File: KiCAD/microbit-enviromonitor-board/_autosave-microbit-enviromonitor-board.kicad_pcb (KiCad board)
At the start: 2 copper layers, 45.7 x 62.2 mm, 12 parts, among them J1 12V, J2 SERIAL, J3 3V3, J4 PUMP, Q1 TIP41C, U1 REGULATOR

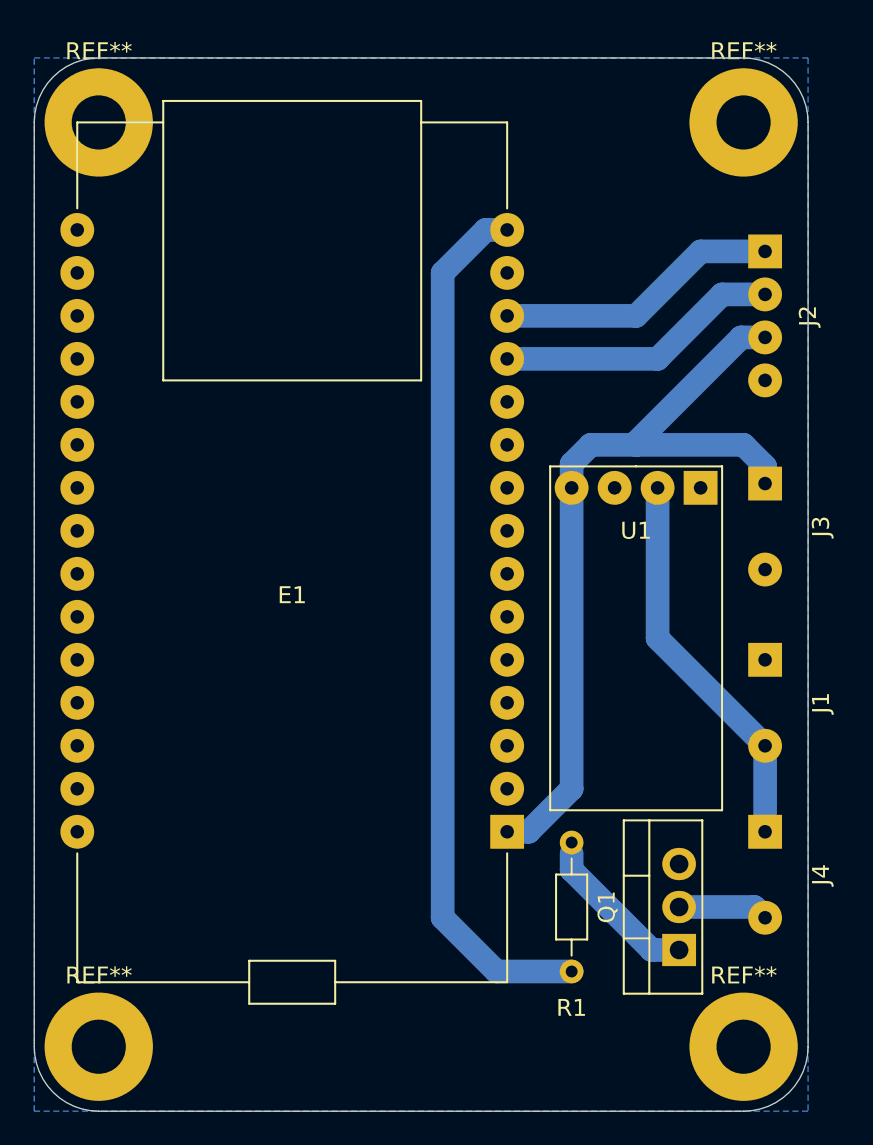
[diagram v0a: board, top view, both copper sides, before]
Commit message: Updated serial port
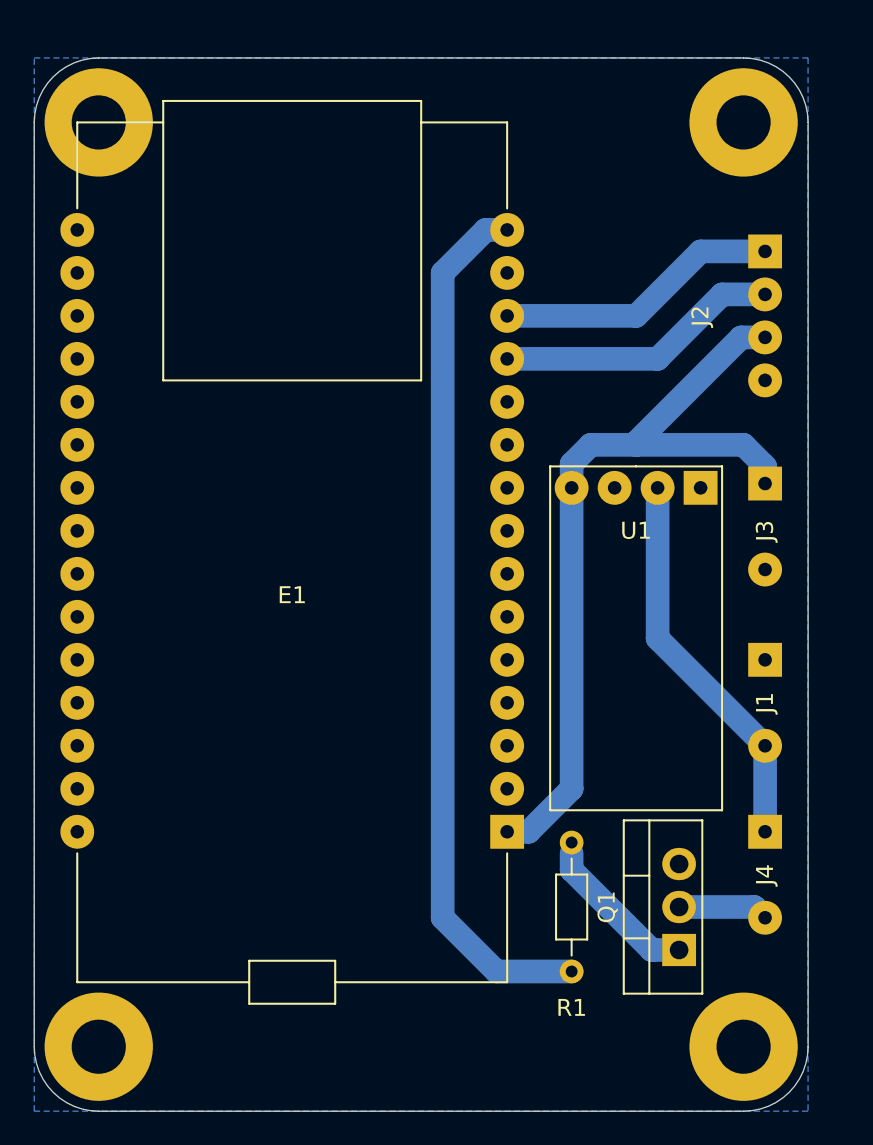
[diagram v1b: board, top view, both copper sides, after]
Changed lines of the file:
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@@
   (module headers:4x1 (layer F.Cu)
     (at 43.18 15.24 270)
-    (fp_text reference J2 (at 0 -2.54 90) (layer F.SilkS)
-      (effects (font (size 1 1) (thickness 0.15)))
-    )
-    (fp_text value SERIAL (at 0 -5.08 90) (layer F.Fab)
+    (fp_text reference J2 (at 0 3.81 90) (layer F.SilkS)
+      (effects (font (size 1 1) (thickness 0.15)))
+    )
+    (fp_text value SERIAL (at 0 2.54 90) (layer F.Fab)
       (effects (font (size 1 1) (thickness 0.15)))
     )
@@
     (tags "mounting hole 3.2mm m3")
     (attr virtual)
-    (fp_text reference REF** (at 0 -4.2) (layer F.SilkS)
-      (effects (font (size 1 1) (thickness 0.15)))
-    )
-    (fp_text value MountingHole_3.2mm_M3_Pad (at 0 4.2) (layer F.Fab)
+    (fp_text reference REF** (at 0 -4.2) (layer F.SilkS) hide
+      (effects (font (size 1 1) (thickness 0.15)))
+    )
+    (fp_text value MountingHole_3.2mm_M3_Pad (at 0 4.2) (layer F.Fab) hide
       (effects (font (size 1 1) (thickness 0.15)))
     )
@@
     (tags "mounting hole 3.2mm m3")
     (attr virtual)
-    (fp_text reference REF** (at 0 -4.2) (layer F.SilkS)
-      (effects (font (size 1 1) (thickness 0.15)))
-    )
-    (fp_text value MountingHole_3.2mm_M3_Pad (at 0 4.2) (layer F.Fab)
+    (fp_text reference REF** (at 0 -4.2) (layer F.SilkS) hide
+      (effects (font (size 1 1) (thickness 0.15)))
+    )
+    (fp_text value MountingHole_3.2mm_M3_Pad (at 0 4.2) (layer F.Fab) hide
       (effects (font (size 1 1) (thickness 0.15)))
     )
@@
     (tags "mounting hole 3.2mm m3")
     (attr virtual)
-    (fp_text reference REF** (at 0 -4.2) (layer F.SilkS)
-      (effects (font (size 1 1) (thickness 0.15)))
-    )
-    (fp_text value MountingHole_3.2mm_M3_Pad (at 0 4.2) (layer F.Fab)
+    (fp_text reference REF** (at 0 -4.2) (layer F.SilkS) hide
+      (effects (font (size 1 1) (thickness 0.15)))
+    )
+    (fp_text value MountingHole_3.2mm_M3_Pad (at 0 4.2) (layer F.Fab) hide
       (effects (font (size 1 1) (thickness 0.15)))
     )
@@
     (tags "mounting hole 3.2mm m3")
     (attr virtual)
-    (fp_text reference REF** (at 0 -4.2) (layer F.SilkS)
-      (effects (font (size 1 1) (thickness 0.15)))
-    )
-    (fp_text value MountingHole_3.2mm_M3_Pad (at 0 4.2) (layer F.Fab)
+    (fp_text reference REF** (at 0 -4.2) (layer F.SilkS) hide
+      (effects (font (size 1 1) (thickness 0.15)))
+    )
+    (fp_text value MountingHole_3.2mm_M3_Pad (at 0 4.2) (layer F.Fab) hide
       (effects (font (size 1 1) (thickness 0.15)))
     )
@@
   (module headers:2_double_spaced (layer F.Cu)
     (at 43.18 48.26 270)
-    (fp_text reference J4 (at 0 -3.31 90) (layer F.SilkS)
+    (fp_text reference J4 (at 0 0 90) (layer F.SilkS)
       (effects (font (size 1 1) (thickness 0.15)))
     )
@@
   (module headers:2_double_spaced (layer F.Cu)
     (at 43.18 27.686 270)
-    (fp_text reference J3 (at 0 -3.31 90) (layer F.SilkS)
+    (fp_text reference J3 (at 0.254 0 90) (layer F.SilkS)
       (effects (font (size 1 1) (thickness 0.15)))
     )
@@
   (module headers:2_double_spaced (layer F.Cu)
     (at 43.18 38.1 270)
-    (fp_text reference J1 (at 0 -3.31 90) (layer F.SilkS)
-      (effects (font (size 1 1) (thickness 0.15)))
-    )
+    (fp_text reference J1 (at 0 0 90) (layer F.SilkS)
+      (effects (font (size 1 1) (thickness 0.15)))
+    )
